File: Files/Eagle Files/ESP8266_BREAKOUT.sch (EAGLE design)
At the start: 17 parts, among them U2 LM1117-3V3-T0-220

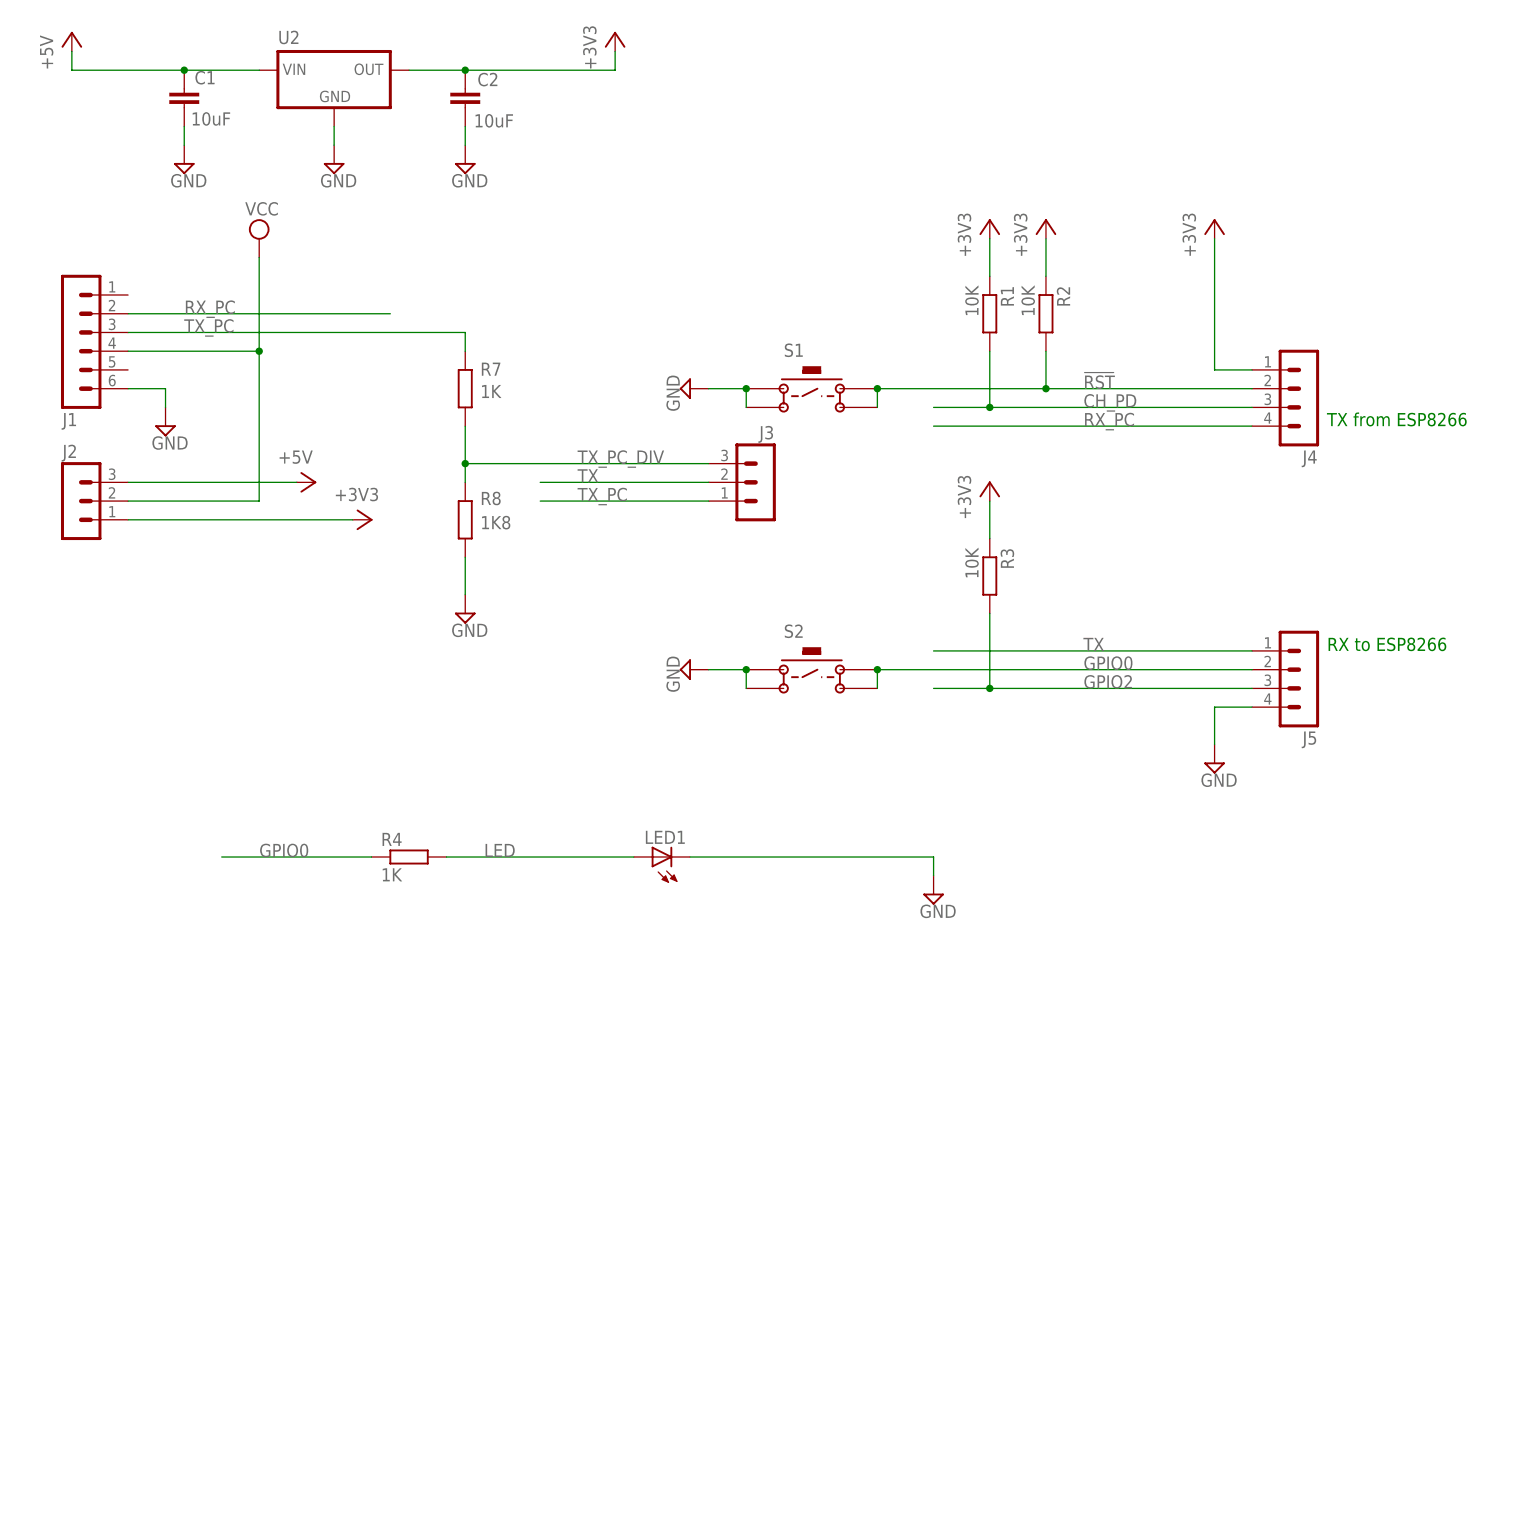
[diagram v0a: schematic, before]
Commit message: My implementation of the ESP8266-01 breakout board
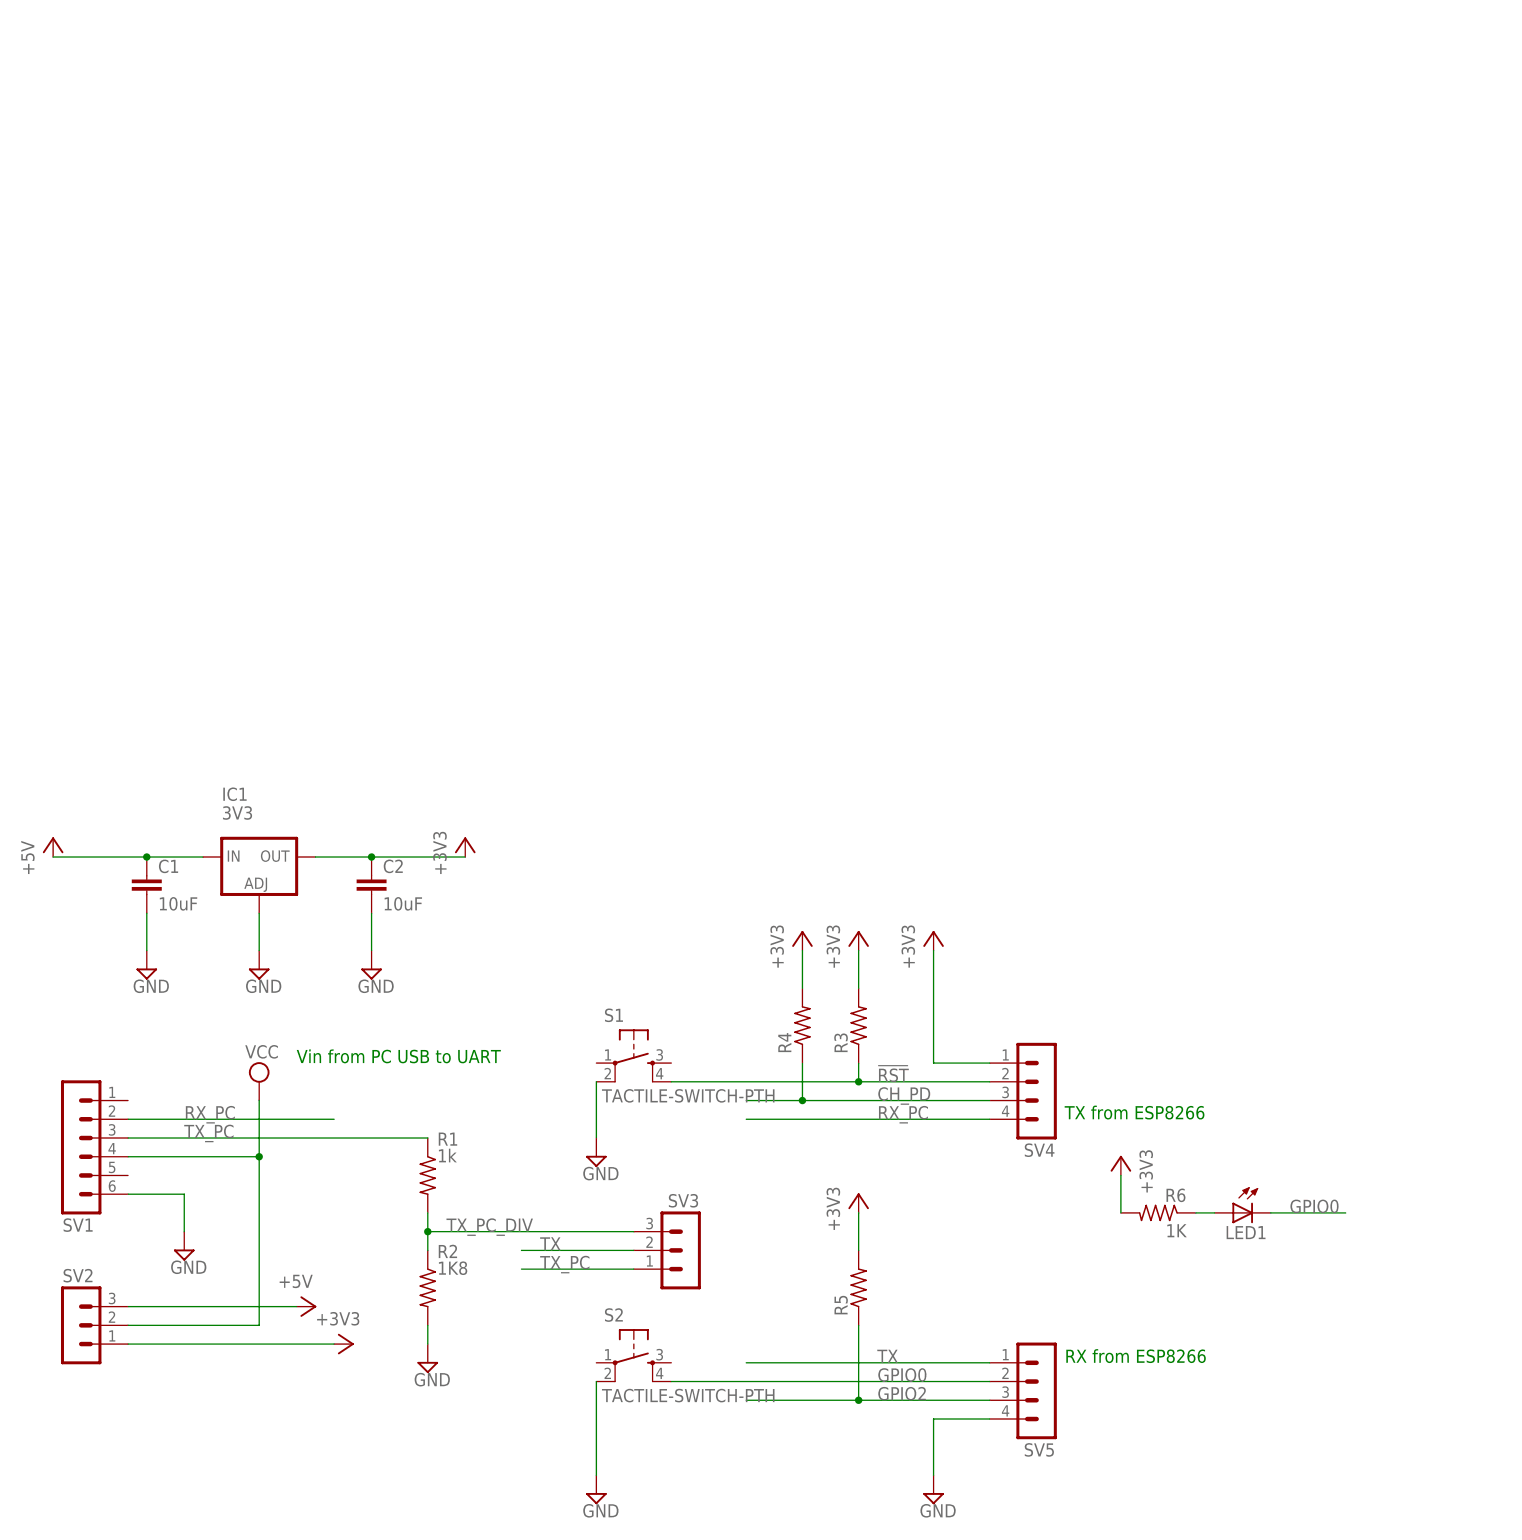
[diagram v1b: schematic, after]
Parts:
- removed J1: (no value), con-lstb:MA06-1
- removed J2, J3: (no value), con-lstb:MA03-1
- removed J4, J5: (no value), con-lstb:MA04-1
- removed R7: 1K, resistor:R-EU_0204_7
- removed R8: 1K8, resistor:R-EU_0204_7
- removed U2: LM1117-3V3-T0-220, LM1117-3V3-TO220:LM1117-3V3-T0-220
- added IC1: 3V3, v-reg:LM317TS
- added R5: (no value), resistor:R-US_0204/7
- added R6: 1K, resistor:R-US_0204/7
- added SV1: (no value), con-lstb:MA06-1
- added SV2, SV3: (no value), con-lstb:MA03-1
- added SV4, SV5: (no value), con-lstb:MA04-1
- R1: value 10K -> 1k; device resistor:R-EU_0204_7 -> resistor:R-US_0204/7
- R2: value 10K -> 1K8; device resistor:R-EU_0204_7 -> resistor:R-US_0204/7
- R3: value 10K -> (none); device resistor:R-EU_0204_7 -> resistor:R-US_0204/7
- R4: value 1K -> (none); device resistor:R-EU_0204_7 -> resistor:R-US_0204/7
- S1, S2: value 1825910-6-SPST-NOPB-4P -> TACTILE-SWITCH-PTH; device 1825910-6:1825910-6-SPST-NOPB-4P -> GeekAmmo:TACTILE-SWITCH-PTH
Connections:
- removed net LED: LED1.A, R4.2
- new net N$1: LED1.A, R6.1
- net !RST: now also R3.1, SV4.2; no longer J4.2, R2.2, S1.3
- net +3V3: now also C2.1, IC1.OUT, R3.2, R4.2, R5.2, R6.2, SV2.1, SV4.1; no longer C2.2, J2.1, J4.1, R1.1, R2.1, R3.1, U2.OUT
- net +5V: now also C1.1, IC1.IN, SV2.3; no longer C1.2, J2.3, U2.IN
- net CH_PD: now also R4.1, SV4.3; no longer J4.3, R1.2
- net GND: now also C1.2, C2.2, IC1.ADJ, R2.2, SV1.6, SV5.4; no longer C1.1, C2.1, J1.6, J5.4, LED1.C, R8.1, S1.1, S2.1, U2.GND
- net GPIO0: now also LED1.C, SV5.2; no longer J5.2, R4.1, S2.3
- net GPIO2: now also R5.1, SV5.3; no longer J5.3, R3.2
- net RX_PC: now also SV1.2, SV4.4; no longer J1.2, J4.4
- net TX: now also SV3.2, SV5.1; no longer J3.2, J5.1
- net TX_PC: now also R1.1, SV1.3, SV3.1; no longer J1.3, J3.1, R7.2
- net TX_PC_DIV: now also R1.2, R2.1, SV3.3; no longer J3.3, R7.1, R8.2
- net VCC: now also SV1.4, SV2.2; no longer J1.4, J2.2
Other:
- note added: "RX from ESP8266"
- note added: "Vin from PC USB to UART"
- note removed: "RX to ESP8266"
- moved on the sheet: C1, C2, LED1
